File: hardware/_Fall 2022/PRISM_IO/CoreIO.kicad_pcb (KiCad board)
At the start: 2 copper layers, 61 x 88.9 mm, 33 parts, among them J1 CORE_FC, J2 COTS_SWITCH_PLUG, J3 PYRO 1, J4 PYRO 2, Q1 AO3400A, Q2 AO3400A

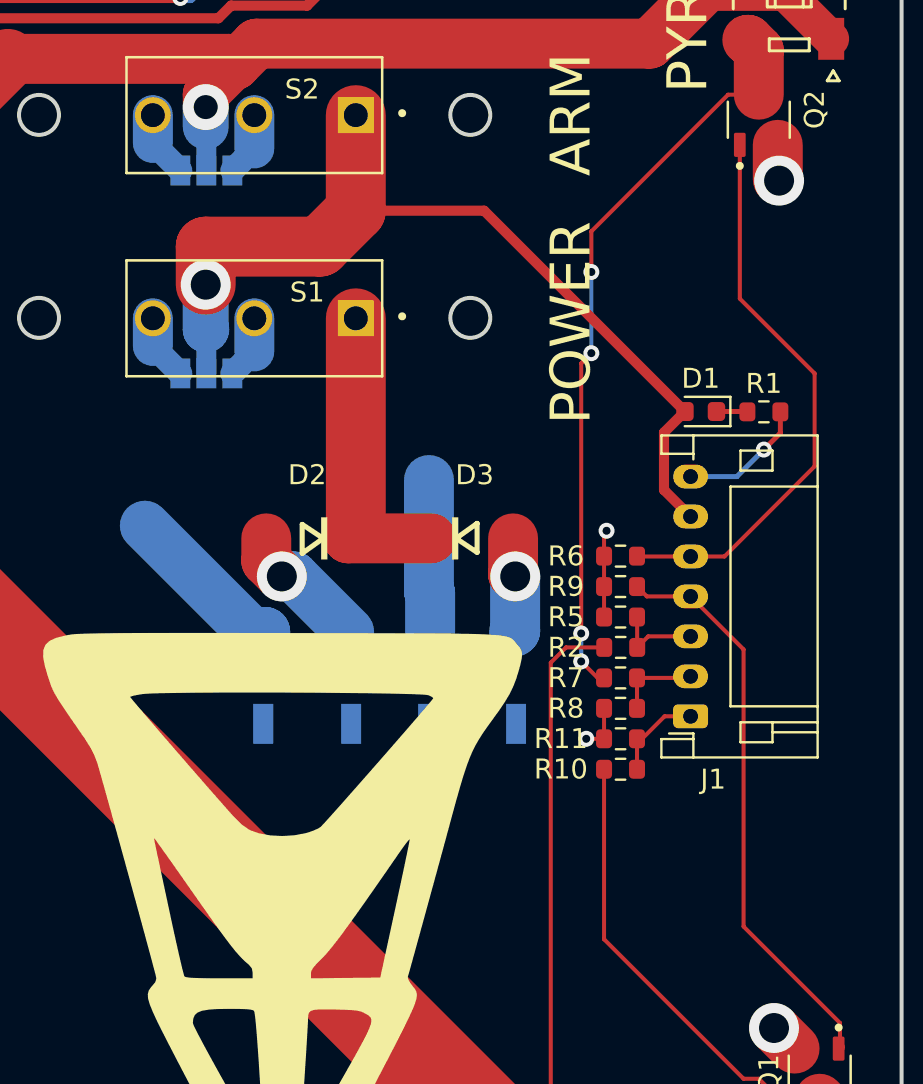
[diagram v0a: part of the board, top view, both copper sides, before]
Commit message: Fix CoreIO board
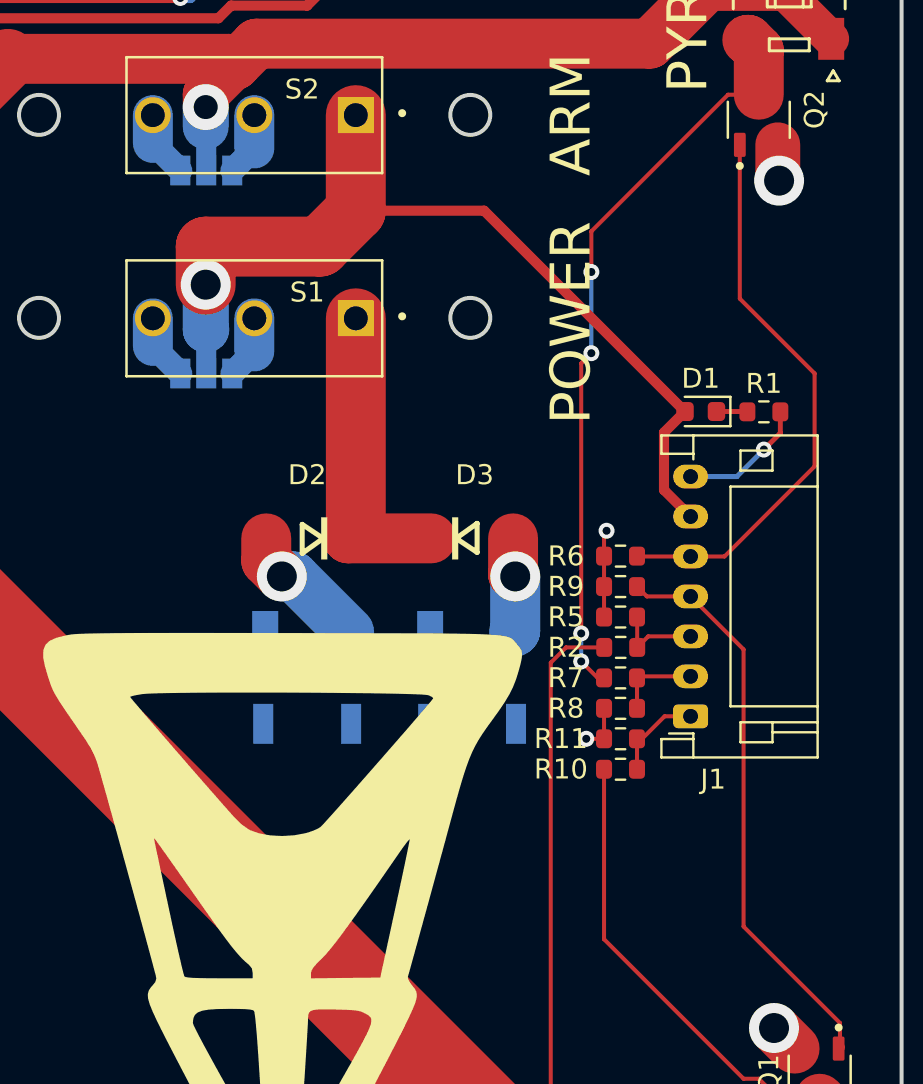
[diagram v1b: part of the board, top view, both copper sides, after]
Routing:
- net GND: track 33.4 -> 16.8 mm
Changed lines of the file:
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@@
     (at 147.32 111.76)
     (attr board_only exclude_from_pos_files exclude_from_bom)
-    (fp_text reference "G***" (at 0 0) (layer "F.SilkS")
+    (fp_text reference "G***" (at 0 0) (layer "F.SilkS") hide
       (effects (font (size 1.524 1.524) (thickness 0.3)))
     )
@@
   (segment (start 165.1 103.632) (end 165.1 102.108) (width 0.2032) (layer "F.Cu") (net 2))
   (segment (start 165.1 102.108) (end 165.354 102.108) (width 0.2032) (layer "F.Cu") (net 2))
-  (segment (start 165.1 99.06) (end 167.701922 99.06) (width 0.2032) (layer "F.Cu") (net 3))
-  (segment (start 167.701922 99.06) (end 167.780605 98.981317) (width 0.508) (layer "F.Cu") (net 3))
-  (segment (start 164.986775 98.981317) (end 164.956928 99.011164) (width 0.2032) (layer "F.Cu") (net 3))
   (segment (start 165.1 100.584) (end 165.1 99.06) (width 0.2032) (layer "F.Cu") (net 3))
+  (segment (start 167.780605 98.981317) (end 165.178683 98.981317) (width 0.2032) (layer "F.Cu") (net 3))
+  (segment (start 165.178683 98.981317) (end 165.1 99.06) (width 0.508) (layer "F.Cu") (net 3))
   (segment (start 165.593317 94.981317) (end 165.1 94.488) (width 0.2032) (layer "F.Cu") (net 4))
   (segment (start 167.780605 94.981317) (end 170.434 97.634712) (width 0.2032) (layer "F.Cu") (net 4))
@@
   (segment (start 172.989 117.617) (end 171.958 116.586) (width 2.5) (layer "F.Cu") (net 7))
   (segment (start 172.275 86.805) (end 171.45 87.63) (width 0.25) (layer "F.Cu") (net 7))
-  (segment (start 172.146 72.375) (end 172.146 74.102) (width 2.5) (layer "F.Cu") (net 7))
+  (segment (start 172.146 72.375) (end 172.146 74.102) (width 2.25) (layer "F.Cu") (net 7))
   (segment (start 163.45 102.108) (end 162.56 102.108) (width 0.2032) (layer "F.Cu") (net 7))
   (segment (start 172.275 85.741317) (end 172.275 86.805) (width 0.25) (layer "F.Cu") (net 7))
@@
   (via (at 162.56 102.108) (size 0.8) (drill 0.4) (layers "F.Cu" "B.Cu") (net 7))
   (via (at 163.576 91.694) (size 0.8) (drill 0.4) (layers "F.Cu" "B.Cu") (net 7))
-  (segment (start 145.782 96.76) (end 140.462 91.44) (width 2.5) (layer "B.Cu") (net 7))
-  (segment (start 154.745 94.801) (end 154.686 94.742) (width 2.5) (layer "B.Cu") (net 7))
-  (segment (start 154.686 94.742) (end 154.686 89.154) (width 2.5) (layer "B.Cu") (net 7))
-  (segment (start 146.49 96.76) (end 146.49 97.468) (width 2.5) (layer "B.Cu") (net 7))
-  (segment (start 154.745 96.76) (end 154.745 94.801) (width 2.5) (layer "B.Cu") (net 7))
-  (segment (start 146.49 96.76) (end 145.782 96.76) (width 2.5) (layer "B.Cu") (net 7))
   (segment (start 170.098683 88.981317) (end 171.45 87.63) (width 0.25) (layer "B.Cu") (net 7))
   (segment (start 167.780605 88.981317) (end 170.098683 88.981317) (width 0.25) (layer "B.Cu") (net 7))
@@
   (segment (start 147.91 93.98) (end 150.69 96.76) (width 2.5) (layer "B.Cu") (net 12))
   (segment (start 147.32 93.98) (end 147.91 93.98) (width 2.5) (layer "B.Cu") (net 12))
+  (segment (start 158.895 93.871) (end 159.004 93.98) (width 2.5) (layer "F.Cu") (net 13))
   (segment (start 158.895 92.075) (end 158.895 93.871) (width 2.5) (layer "F.Cu") (net 13))
-  (segment (start 158.895 93.871) (end 159.004 93.98) (width 2.5) (layer "F.Cu") (net 13))
   (via (at 159.004 93.98) (size 2.5) (drill 1.5) (layers "F.Cu" "B.Cu") (net 13))
+  (segment (start 159.004 96.701) (end 158.945 96.76) (width 2.5) (layer "B.Cu") (net 13))
   (segment (start 159.004 93.98) (end 159.004 96.701) (width 2.5) (layer "B.Cu") (net 13))
-  (segment (start 159.004 96.701) (end 158.945 96.76) (width 2.5) (layer "B.Cu") (net 13))
   (segment (start 169.076105 85.725) (end 170.608683 85.725) (width 0.25) (layer "F.Cu") (net 14))
   (segment (start 170.608683 85.725) (end 170.625 85.741317) (width 0.25) (layer "F.Cu") (net 14))

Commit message: PRISM_IO gerbers
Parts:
- added ?: MountingHole_2.2mm_M2, MountingHole:MountingHole_2.2mm_M2, F.Cu at (135.2, 70.9)
- added REF**: MountingHole_2.2mm_M2, MountingHole:MountingHole_2.2mm_M2, F.Cu at (156.8, 70.9)
- added REF**: MountingHole_2.2mm_M2, MountingHole:MountingHole_2.2mm_M2, F.Cu at (135.2, 60.7)
- added REF**: MountingHole_2.2mm_M2, MountingHole:MountingHole_2.2mm_M2, F.Cu at (135.2, 81.0)
- added REF**: MountingHole_2.2mm_M2, MountingHole:MountingHole_2.2mm_M2, F.Cu at (156.8, 81.0)
- added REF**: MountingHole_2.2mm_M2, MountingHole:MountingHole_2.2mm_M2, F.Cu at (156.8, 60.7)
- moved G*** 0.46 mm to (147.8, 111.8)
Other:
- outline, holes or cut-outs redrawn
- board text added: "Ari Bobesh Charlie Babe Jiayuan Liu Lili Baker Rowan Jansens"
